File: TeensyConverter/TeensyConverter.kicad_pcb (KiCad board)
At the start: 2 copper layers, 5 parts, among them J1 Conn_01x03, U1 Teensy-3.2, U2 CE_Header

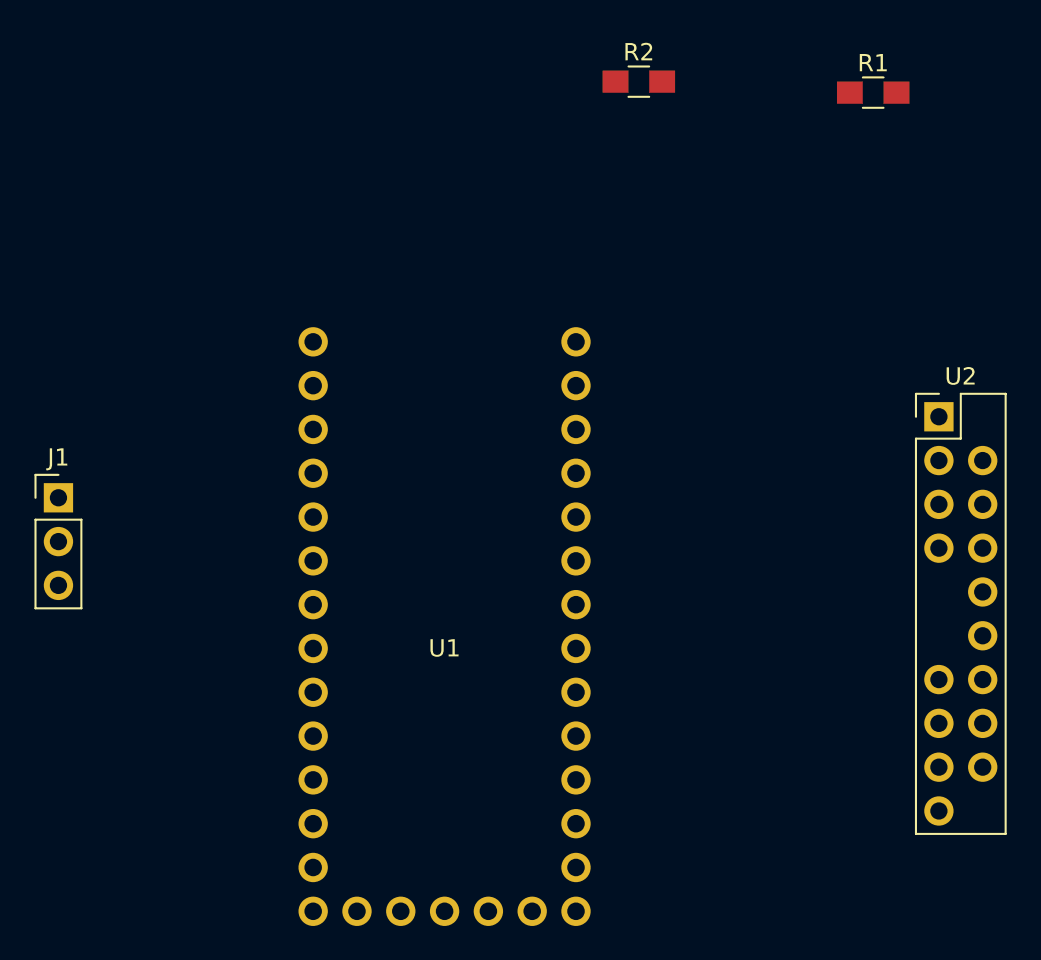
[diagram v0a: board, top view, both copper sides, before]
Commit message: Flipped Teensy schematic and started netlist placement
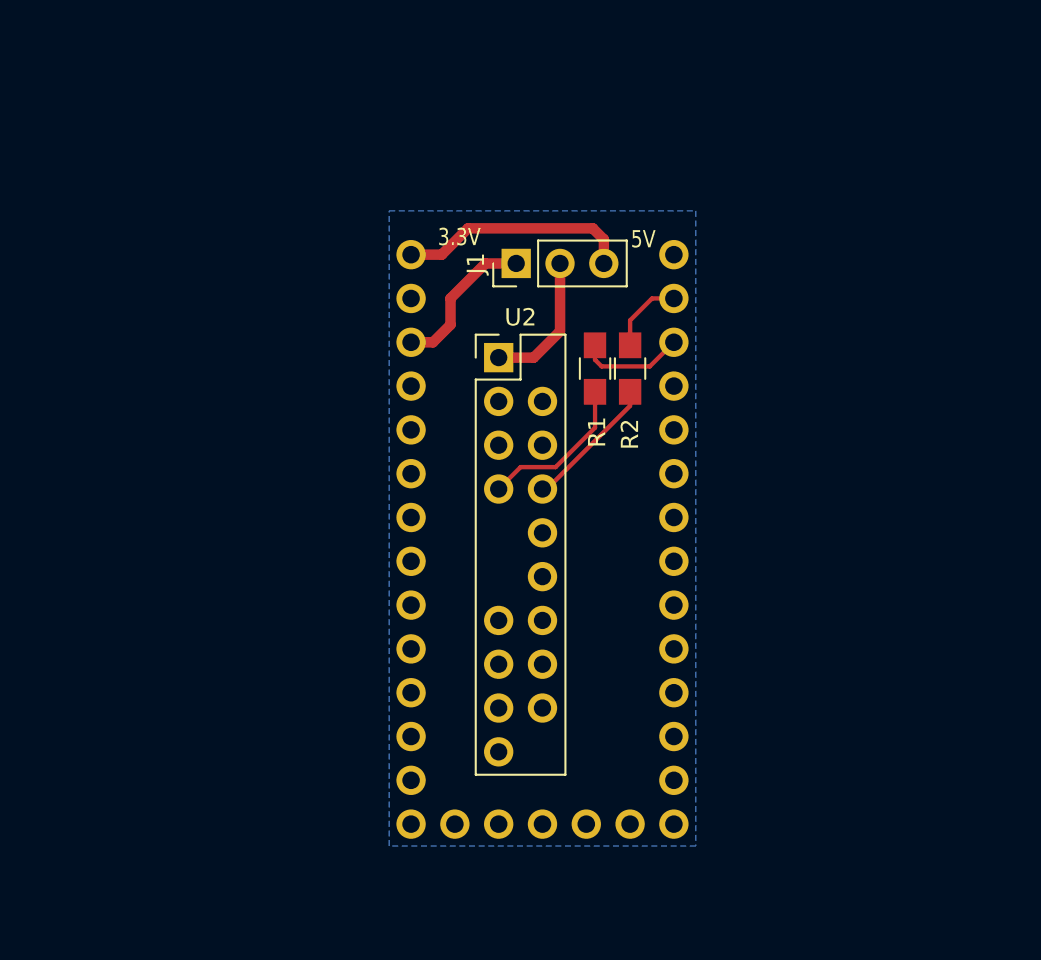
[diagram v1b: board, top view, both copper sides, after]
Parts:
- U1: moved to B.Cu
- moved J1 29.8 mm to (152.7, 85.2), turned to 90 degrees
- moved U2 25.8 mm to (151.6, 90.7)
- moved R1 22.7 mm to (157.2, 91.3), turned to 90 degrees
- moved R2 16.6 mm to (159.3, 91.3), turned to 270 degrees
- moved U1 7.60 mm to (154.2, 99.9), turned to 180 degrees
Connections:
- U1 pad 30: Net-(U1-Pad30) -> /GND
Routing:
- net /5V: track 0.00 -> 13.5 mm
- net /DEVICE_RX: track 0.00 -> 9.14 mm
- net /3.3V: track 0.00 -> 8.88 mm
- net Net-(J1-Pad2): track 0.00 -> 8.12 mm
- net /DEVICE_TX: track 0.00 -> 7.89 mm
- net /TEENSY_TX: track 0.00 -> 6.15 mm
- net /TEENSY_RX: track 0.00 -> 4.51 mm
- added copper zone on B.Cu, net /GND
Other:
- net class Default: clearance 0.2 -> 0.1524; trace_width 0.25 -> 0.254; via_dia 0.6 -> 0.6858; via_drill 0.4 -> 0.3302
- rule trace_clearance: 0.2 -> 0.1524
- rule trace_min: 0.2 -> 0.1524
- rule via_min_drill: 0.3 -> 0.3302
- rule via_min_size: 0.4 -> 0.6858
- board text added: "3.3V"
- board text added: "5V"
